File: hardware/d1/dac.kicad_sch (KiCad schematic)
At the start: 4 parts, among them CN1 PJ-3255A, U1 CS43131-CNZR, X2 OT7EL89CJI-111YLC-24_576M

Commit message: New components
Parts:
- added R1: 10k, Resistor_SMD:R_0603_1608Metric, symbol Device:R_Small
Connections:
- net I2S_WS: now also U1.38 (LRCK1)
- no-connect marks 1 -> 4
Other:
- note added: "Has internal pull-down"
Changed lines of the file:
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@@
 	(generator_version "10.0")
 	(paper "A4")
+	(text "Has internal\npull-down"
+		(exclude_from_sim no)
+		(at 110.998 92.964 0)
+		(effects
+			(font
+				(size 1.27 1.27)
+			)
+		)
+	)
 	(no_connect
 		(at 118.11 82.55)
+	)
+	(no_connect
+		(at 118.11 90.17)
+	)
+	(no_connect
+		(at 118.11 92.71)
+	)
+	(no_connect
+		(at 118.11 95.25)
 	)
 	(wire
@@
 	)
 	(label "I2S_WS"
-		(at 165.1 92.71 0)
+		(at 163.83 92.71 0)
 		(effects
 			(font
@@
 		)
 	)
+	(symbol
+		(lib_id "Device:R_Small")
+		(at 73.66 43.18 90)
+		(unit 1)
+		(body_style 1)
+		(exclude_from_sim no)
+		(in_bom yes)
+		(on_board yes)
+		(in_pos_files yes)
+		(dnp no)
+		(property "Reference" "R1"
+			(at 69.088 43.18 90)
+			(show_name no)
+			(do_not_autoplace no)
+			(effects
+				(font
+					(size 1.016 1.016)
+				)
+			)
+		)
+		(property "Value" "10k"
+			(at 73.66 43.18 90)
+			(show_name no)
+			(do_not_autoplace no)
+			(effects
+				(font
+					(size 1.27 1.27)
+				)
+			)
+		)
+		(property "Footprint" "Resistor_SMD:R_0603_1608Metric"
+			(at 73.66 43.18 0)
+			(hide yes)
+			(show_name no)
+			(do_not_autoplace no)
+			(effects
+				(font
+					(size 1.27 1.27)
+				)
+			)
+		)
+		(property "Datasheet" ""
+			(at 73.66 43.18 0)
+			(hide yes)
+			(show_name no)
+			(do_not_autoplace no)
+			(effects
+				(font
+					(size 1.27 1.27)
+				)
+			)
+		)
+		(property "Description" "Resistor, small symbol"
+			(at 73.66 43.18 0)
+			(hide yes)
+			(show_name no)
+			(do_not_autoplace no)
+			(effects
+				(font
+					(size 1.27 1.27)
+				)
+			)
+		)
+		(pin "2"
+		)
+		(pin "1"
+		)
+		(instances
+			(project "DrunkEarPhoneAdapter"
+				(path "/df940915-8af0-46f9-b18a-23d4684ae671/95ba76fd-cd0d-4fc7-9d47-f5665dc7e9c9"
+					(reference "R1")
+					(unit 1)
+				)
+			)
+		)
+	)

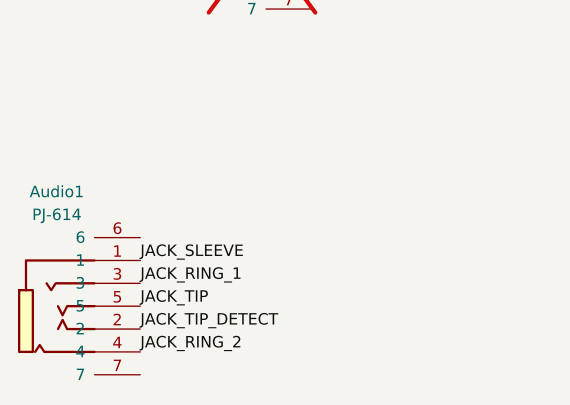
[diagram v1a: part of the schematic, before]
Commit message: Change uart pins, add components
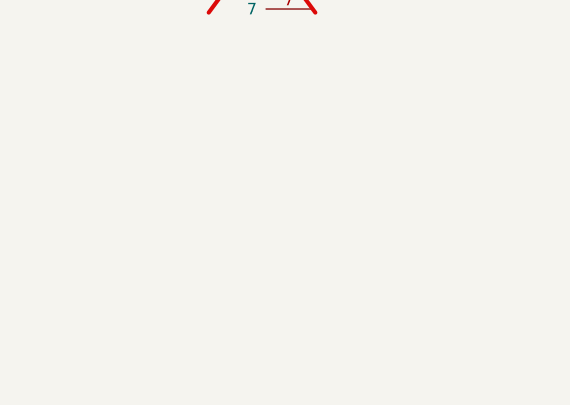
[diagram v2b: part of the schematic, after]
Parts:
- removed Audio1: PJ-614, JLCImport:PJ-614, symbol JLCImport:PJ-614
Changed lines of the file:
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@@
-		)
-	)
-	(label "JACK_SLEEVE"
-		(at 63.5 133.35 0)
-		(effects
-			(font
-				(size 1.27 1.27)
-			)
-			(justify left bottom)
 		)
 	)
@@
 		)
 	)
-	(label "JACK_TIP"
-		(at 63.5 138.43 0)
-		(effects
-			(font
-				(size 1.27 1.27)
-			)
-			(justify left bottom)
-		)
-	)
 	(label "JACK_TIP_DETECT"
 		(at 172.72 74.93 0)
@@
 		)
 	)
-	(label "JACK_RING_2"
-		(at 63.5 143.51 0)
-		(effects
-			(font
-				(size 1.27 1.27)
-			)
-			(justify left bottom)
-		)
-	)
 	(label "I2C_SCL"
 		(at 118.11 59.69 180)
@@
 			)
 			(justify right bottom)
-		)
-	)
-	(label "JACK_TIP_DETECT"
-		(at 63.5 140.97 0)
-		(effects
-			(font
-				(size 1.27 1.27)
-			)
-			(justify left bottom)
-		)
-	)
-	(label "JACK_RING_1"
-		(at 63.5 135.89 0)
-		(effects
-			(font
-				(size 1.27 1.27)
-			)
-			(justify left bottom)
 		)
 	)
@@
 					(unit 1)
 				)
-			)
-		)
-	)
-	(symbol
-		(lib_id "JLCImport:PJ-614")
-		(at 57.15 137.16 0)
-		(unit 1)
-		(body_style 1)
-		(exclude_from_sim no)
-		(in_bom yes)
-		(on_board yes)
-		(in_pos_files yes)
-		(dnp no)
-		(fields_autoplaced yes)
-		(property "Reference" "Audio1"
-			(at 54.229 125.73 0)
-			(show_name no)
-			(do_not_autoplace no)
-			(effects
-				(font
-					(size 1.27 1.27)
-				)
-			)
-		)
-		(property "Value" "PJ-614"
-			(at 54.229 128.27 0)
-			(show_name no)
-			(do_not_autoplace no)
-			(effects
-				(font
-					(size 1.27 1.27)
-				)
-			)
-		)
-		(property "Footprint" "JLCImport:PJ-614"
-			(at 57.15 137.16 0)
-			(hide yes)
-			(show_name no)
-			(do_not_autoplace no)
-			(effects
-				(font
-					(size 1.27 1.27)
-				)
-			)
-		)
-		(property "Datasheet" "https://www.lcsc.com/datasheet/lcsc_datasheet_2108131730_Korean-Hroparts-Elec-PJ-614_C145801.pdf"
-			(at 57.15 137.16 0)
-			(hide yes)
-			(show_name no)
-			(do_not_autoplace no)
-			(effects
-				(font
-					(size 1.27 1.27)
-				)
-			)
-		)
-		(property "Description" "12V 1A 3.5mm Headphone Jack Copper alloy Gold SMD Audio Connectors ROHS"
-			(at 57.15 137.16 0)
-			(hide yes)
-			(show_name no)
-			(do_not_autoplace no)
-			(effects
-				(font
-					(size 1.27 1.27)
-				)
-			)
-		)
-		(property "LCSC" "C145801"
-			(at 57.15 137.16 0)
-			(hide yes)
-			(show_name no)
-			(do_not_autoplace no)
-			(effects
-				(font
-					(size 1.27 1.27)
-				)
-			)
-		)
-		(property "Manufacturer" "Korean Hroparts Elec"
-			(at 57.15 137.16 0)
-			(hide yes)
-			(show_name no)
-			(do_not_autoplace no)
-			(effects
-				(font
-					(size 1.27 1.27)
-				)
-			)
-		)
-		(property "Manufacturer Part" "PJ-614"
-			(at 57.15 137.16 0)
-			(hide yes)
-			(show_name no)
-			(do_not_autoplace no)
-			(effects
-				(font
-					(size 1.27 1.27)
-				)
-			)
-		)
-		(pin "1"
-		)
-		(pin "2"
-		)
-		(pin "3"
-		)
-		(pin "4"
-		)
-		(pin "7"
-		)
-		(pin "6"
-		)
-		(pin "5"
-		)
-		(instances
-			(project "DrunkEarPhoneAdapter"
-				(path "/df940915-8af0-46f9-b18a-23d4684ae671/95ba76fd-cd0d-4fc7-9d47-f5665dc7e9c9"
-					(reference "Audio1")
-					(unit 1)
-				)

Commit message: Add new parts
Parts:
- removed R1: 10k, Resistor_SMD:R_0603_1608Metric, symbol Device:R_Small
- added C16: 4.7uF 10V X5R, JLCImport:CL05A475MP5NRNC, symbol JLCImport:CL05A475MP5NRNC
- added C17: 1uF 25V X5R, JLCImport:CL05A105KA5NQNC, symbol JLCImport:CL05A105KA5NQNC
- added C19, C21, C22, C23, C24: 100nF 16V X7R, JLCImport:CL05B104KO5NNNC, symbol JLCImport:CL05B104KO5NNNC
- added C25, C28, C29, C30, C31, C32, C33, C34: 2.2uF 16V X5R, JLCImport:CL05A225KO5NQNC, symbol JLCImport:CL05A225KO5NQNC
- added C26, C27: 15uF 35V X5R, JLCImport:C2012X5R1V156MT000E, symbol JLCImport:C2012X5R1V156MT000E
- added L1, L3: BLM15AG601SN1D, JLCImport:BLM15AG601SN1D, symbol JLCImport:BLM15AG601SN1D
- added U14: BLM15PX601SN1D, JLCImport:BLM15PX601SN1D, symbol JLCImport:BLM15PX601SN1D
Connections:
- net GND: now reaches X2.2 (GND)
- net GND: now also U1.35 (GNDD), U1.41 (EP), U1.8 (GNDA), C16.2, C17.1, C19.2, C21.1, C22.2, C23.1, C24.2, C25.2, C28.2, C30.2
- net at X2.4 (VDD): now also C17.2, C19.1, L1.2
- net FLYP_VA: now reaches U1.10 (FLYP_VA)
- net FLYP_VA: now also C29.1
- net FLYN_VA: now reaches U1.11 (FLYN_VA)
- net FLYN_VA: now also C29.2
- net VCP_FILT-: now reaches U1.18 (VCP_FILT–)
- net VCP_FILT-: now also C32.2
- net GNDCP: now reaches U1.19 (GNDCP)
- net GNDCP: now also C31.2, C32.1
- net FLYN_VCP: now reaches U1.20 (FLYN_VCP)
- net FLYN_VCP: now also C34.1
- net VCP_FILT+: now reaches U1.21 (VCP_FILT+)
- net VCP_FILT+: now also C31.1
- net FLYC_VCP: now reaches U1.23 (FLYC_VCP)
- net FLYC_VCP: now also C33.2, C34.2
- net FLYP_VCP: now reaches U1.24 (FLYP_VCP)
- net FLYP_VCP: now also C33.1
- net VCP: now reaches U1.25 (VCP)
- net VCP: now also C30.1
- net at U1.26 (VP): now also C16.1, C21.2, U14.2
- net DAC_RESET: now reaches U1.28 (RESET#)
- net at U1.31 (VL): now also U1.4 (VD), C22.1, C24.1, L3.2
- net FILT+: now reaches U1.5 (FILT+)
- net FILT+: now also C26.1
- net FILT-: now reaches U1.6 (FILT–)
- net FILT-: now also C27.2
- net +1V8_A: now reaches U1.7 (VA)
- net +1V8_A: now also C23.2, C25.1, C26.2
- net -VA: now reaches U1.9 (-VA)
- net -VA: now also C27.1, C28.1
- net JACK_SLEEVE renamed JACK_DETECTED_GND
- new net +1V8_D: L1.1, L3.1
- new net +3V8: U14.1
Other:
- note added: "Not using now pins has internal pull-down"
- note added: "Using oscilator"
- note removed: "Has internal pull-down"
- moved on the sheet: CN1

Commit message: Pre-finalize sch
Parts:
- removed CN1: PJ-3255A, JLCImport:PJ-3255A, symbol JLCImport:PJ-3255A
- removed X2: OT7EL89CJI-111YLC-24_576M, JLCImport:OT7EL89CJI-111YLC-24_576M, symbol JLCImport:OT7EL89CJI-111YLC-24_576M
- added C76: 1uF 25V X5R, JLCImport:CL05A105KA5NQNC, symbol JLCImport:CL05A105KA5NQNC
- added C77, C78, C79: 100nF 16V X7R, JLCImport:CL05B104KO5NNNC, symbol JLCImport:CL05B104KO5NNNC
- added R1, R7, R9: 33Ω, Resistor_SMD:R_0402_1005Metric, symbol JLCImport:RC0402FR-0733RL
- added R4, R6: 100kΩ, JLCImport:0402WGF1003TCE, symbol JLCImport:0402WGF1003TCE
- added R5, R8: 10kΩ, Resistor_SMD:R_0402_1005Metric, symbol JLCImport:0402WGF1002TCE
- added U18, U19: TPS22917DBVR, JLCImport:TPS22917DBVR, symbol JLCImport:TPS22917DBVR
- added X1: 22.5792MHz, JLCImport:SX2M22_5792M20F30TNN, symbol JLCImport:SX2M22_5792M20F30TNN
- added X3: 24.576MHz, JLCImport:SX2M22_5792M20F30TNN, symbol JLCImport:SX2M22_5792M20F30TNN
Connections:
- net GNDCP is gone; now on net GND: C31.2, C32.1, U1.19 (GNDCP)
- net +1V8_D: now also R4.2, R6.2
- net DAC_RESET: now also R4.1
- net GND: now also U1.30 (ADR), U1.36 (XTO), C76.1, C77.2, C78.2, C79.2, R5.1, R8.1, U18.2 (GND), U19.2 (GND), X1.2 (GND), X3.2 (GND)
- net at C17.2, C19.1: now also U18.5 (QOD), U18.6 (VOUT), X3.1 (OE/NC), X3.4 (VDD); no longer L1.2
- net at U1.37 (XTI/MCLK): now also R1.2, R7.2
- net /INT: now reaches U1.27 (INT#)
- net /INT: now also R6.1
- net at U1.33 (CLKOUT): now also R9.1
- net JACK_DETECTED_GND renamed JACK_RING_2
- net VCP renamed +1V8_CP
- new net: C78.1, C79.1, L1.2, U18.1 (VIN), U19.1 (VIN)
- new net: C76.2, C77.1, U19.5 (QOD), U19.6 (VOUT), X1.1 (OE/NC), X1.4 (VDD)
- new net: R7.1, X3.3 (OUT)
- new net: R1.1, X1.3 (OUT)
- new net CLKOUT: R9.2
- new net CLOCK_EN_22_5792: R8.2, U19.3 (ON)
- new net CLOCK_EN_24_576: R5.2, U18.3 (ON)
- no-connect marks 4 -> 6
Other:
- note added: "Disabled by default"
- note added: "I2C addr: 0x30"
- note added: "Need to be two separate connections"
- moved on the sheet: C16, C21, C22, C23, C24, C25, C30, L1, L3, U1, U14

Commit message: Fixes
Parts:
- removed R1, R7: 33Ω, Resistor_SMD:R_0402_1005Metric, symbol JLCImport:RC0402FR-0733RL
- added U17: SN74LVC1G32DBVR, Package_TO_SOT_SMD:SOT-23-5, symbol JLCImport:SN74LVC1G32DBVR
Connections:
- net GND: now also U17.3 (GND)
- net at C78.1, C79.1, L1.2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: now also U17.5 (VCC)
- net at X3.3 (OUT): now also U17.1 (A)
- net at U1.37 (XTI/MCLK): now also U17.4 (Y)
- net at X1.3 (OUT): now also U17.2 (B)
- net DAC_RESET renamed DAC_RESET/

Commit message: Pre power change
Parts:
- added R35: 1kΩ, Resistor_SMD:R_0402_1005Metric, symbol JLCImport:RC0402FR-071KL
- added U20: SN74AVC4T774RSVR, JLCImport:SN74AVC4T774RSVR, symbol JLCImport:SN74AVC4T774RSVR
- added U21: TCA9406DCUR, JLCImport:TCA9406DCUR, symbol JLCImport:TCA9406DCUR
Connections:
- net JACK_TIP_DETECT: now also R35.2; no longer U1.22 (HP_DETECT)
- new net: R35.1, U1.22 (HP_DETECT)

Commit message: Fixes
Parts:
- removed R5, R8: 10kΩ, Resistor_SMD:R_0402_1005Metric, symbol JLCImport:0402WGF1002TCE
- added C89, C90, C91, C92: 100nF 16V X7R, JLCImport:CL05B104KO5NNNC, symbol JLCImport:CL05B104KO5NNNC
- added R5, R7: 100kΩ, JLCImport:0402WGF1003TCE, symbol JLCImport:0402WGF1003TCE
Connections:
- net +1V8_D: now also U20.14 (VCCA), U20.15 (DIR1), U20.16 (DIR2), U20.5 (DIR3), U21.3 (VCCA), U21.6 (OE), C89.2, C92.2; no longer R4.2, R6.2
- net CLOCK_EN_22_5792: now also R7.2
- net CLOCK_EN_24_576: now also R5.2
- net DAC_RESET/: now also R4.2; no longer R4.1
- net GND: now also R4.1, U20.6 (DIR4), U20.7 (#OE), U20.8 (GND), U21.2 (GND), C89.1, C90.2, C91.1, C92.1, R5.1, R7.1
- net I2C_SCL: now also U21.8 (SCL_B); no longer U1.1 (SCL)
- net I2C_SDA: now also U21.1 (SDA_B); no longer U1.39 (SDA)
- net I2S_CK: now also U20.12 (B1); no longer U1.34 (SCLK1)
- net I2S_SD: now also U20.9 (B4); no longer U1.2 (SDIN1)
- net I2S_WS: now also U20.11 (B2); no longer U1.38 (LRCK1)
- net at R9.1: now also U20.10 (B3); no longer U1.33 (CLKOUT)
- net I2S_CK_1v8: now reaches U20.1 (A1)
- net I2S_CK_1v8: now also U1.34 (SCLK1)
- net +3V3_D: now reaches U20.13 (VCCB)
- net +3V3_D: now also R6.2, U21.7 (VCCB), C90.1, C91.2
- net I2S_WS_1v8: now reaches U20.2 (A2)
- net I2S_WS_1v8: now also U1.38 (LRCK1)
- net CLKOUT_1v8: now reaches U20.3 (A3)
- net CLKOUT_1v8: now also U1.33 (CLKOUT)
- net I2S_SD_1v8: now reaches U20.4 (A4)
- net I2S_SD_1v8: now also U1.2 (SDIN1)
- net I2C_SDA_1v8: now reaches U21.4 (SDA_A)
- net I2C_SDA_1v8: now also U1.39 (SDA)
- net I2C_SCL_1v8: now reaches U21.5 (SCL_A)
- net I2C_SCL_1v8: now also U1.1 (SCL)
- no-connect marks 6 -> 8
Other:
- moved on the sheet: C31, C32, C33, C34, U20, U21

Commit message: Fixesss
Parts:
- added C93, C94: 1uF 25V X5R, JLCImport:CL05A105KA5NQNC, symbol JLCImport:CL05A105KA5NQNC
- added R16, R38: 33Ω, Resistor_SMD:R_0402_1005Metric, symbol JLCImport:RC0402FR-0733RL
- added R37, R8: 100kΩ, JLCImport:0402WGF1003TCE, symbol JLCImport:0402WGF1003TCE
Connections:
- net GND: now also C93.2, C94.2, R37.1, R8.1
- net I2S_CK: now also R38.2; no longer U20.12 (B1)
- net at U17.1 (A), X3.3 (OUT): now also R37.2
- net at U17.2 (B), X1.3 (OUT): now also R8.2
- net at U17.4 (Y): now also R16.1; no longer U1.37 (XTI/MCLK)
- net at C78.1, C79.1, L1.2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: now also C93.1, C94.1
- new net: R38.1, U20.12 (B1)
- new net: R16.2, U1.37 (XTI/MCLK)
